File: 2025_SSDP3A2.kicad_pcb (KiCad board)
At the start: 4 copper layers, 58.4 x 28.8 mm, 64 parts, among them J1 SolderPad, J2 SolderPad, J3 SolderPad, J4 SolderPad, J5 SolderPad, J6 SolderPad, J7 SolderPad_01x06, Q1 IAUZ30N10S5L240, Q2 BSZ096N10LS5, U1 LM5146RGYR

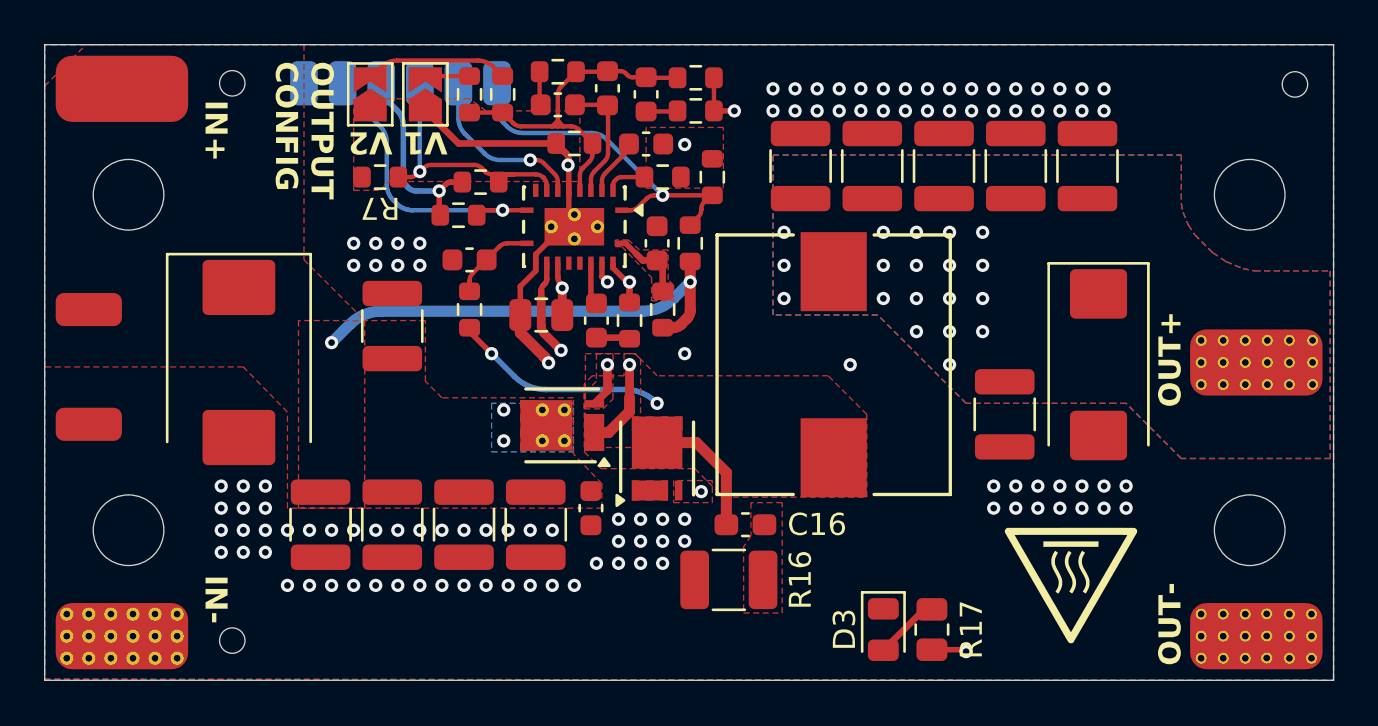
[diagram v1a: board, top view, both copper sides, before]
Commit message: Improvements to copper, EMI reduction techniques
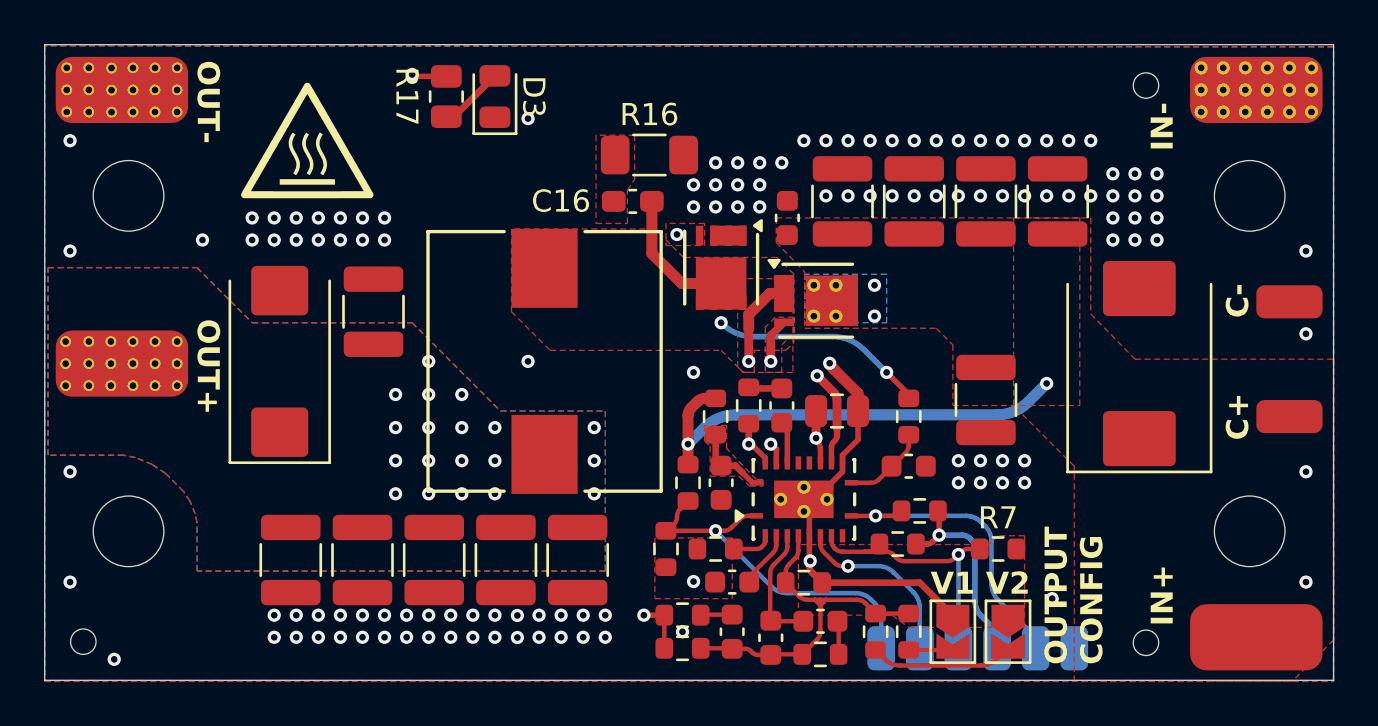
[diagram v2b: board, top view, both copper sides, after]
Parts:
- R16: footprint Resistor_SMD:R_1210_3225Metric_Pad1.30x2.65mm_HandSolder -> Resistor_SMD:R_1206_3216Metric_Pad1.30x1.75mm_HandSolder
- moved H5 60.4 mm to (121.8, 127.0), turned to 180 degrees
- moved J1 57.1 mm to (174.9, 126.8), turned to -90 degrees
- moved J4 57.0 mm to (174.9, 102.0), turned to -90 degrees
- moved J6 57.0 mm to (123.5, 102.0), turned to 90 degrees
- moved J3 54.7 mm to (176.4, 111.7), turned to -90 degrees
- moved J2 54.6 mm to (176.4, 116.8), turned to -90 degrees
- moved H1 53.0 mm to (174.6, 122.0), turned to 180 degrees
- moved H3 53.0 mm to (123.8, 122.0), turned to 180 degrees
- moved H2 53.0 mm to (174.6, 106.8), turned to 180 degrees
- moved H4 53.0 mm to (123.8, 106.8), turned to 180 degrees
- moved J5 51.4 mm to (123.5, 114.5), turned to 90 degrees
- moved H6 48.5 mm to (169.9, 127.1), turned to 180 degrees
- moved H7 48.4 mm to (169.9, 101.8), turned to 180 degrees
- moved D1 40.8 mm to (169.6, 114.5), turned to 90 degrees
- moved C22 40.3 mm to (131.2, 123.3), turned to -90 degrees
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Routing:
- net PGND: vias 108 -> 121
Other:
- board text added: "C+"
- board text added: "C-"
- board text added: "INPUT: 20-60V⎓4A OUTPUT: 5.1-12V⎓8A"
- board text removed: "INPUT: 20-70V⎓4A OUTPUT: 5.1-12V⎓8A"

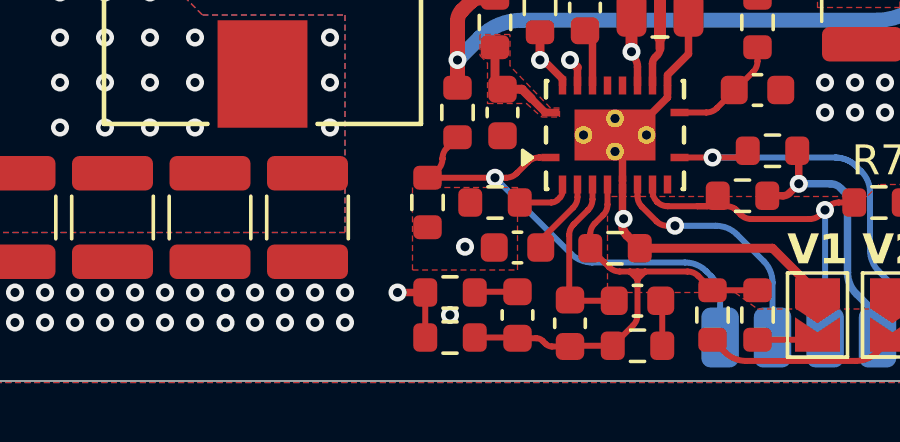
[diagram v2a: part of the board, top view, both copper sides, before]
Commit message: Updated schematic, added more silkscreen markings
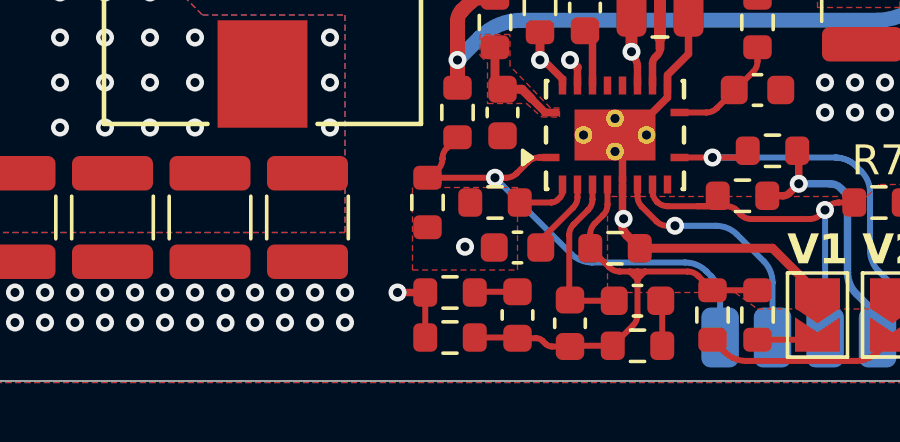
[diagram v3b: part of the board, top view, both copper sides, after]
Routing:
- net PGND: vias 121 -> 120
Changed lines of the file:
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@@
-	)
-	(via
-		(at 148.9 126.6)
-		(size 0.6)
-		(drill 0.3)
-		(layers "F.Cu" "B.Cu")
-		(free yes)
-		(net 1)
 	)
 	(via

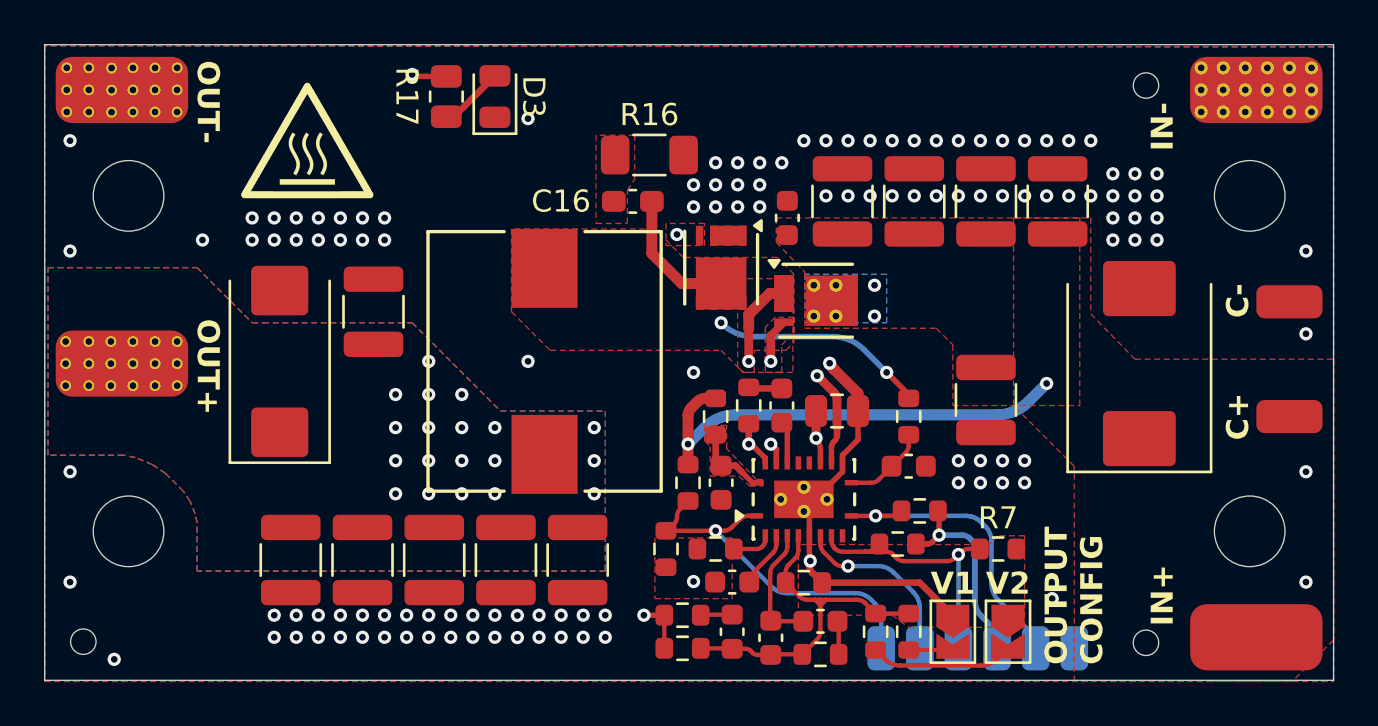
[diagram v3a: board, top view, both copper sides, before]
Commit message: Added more thermal area
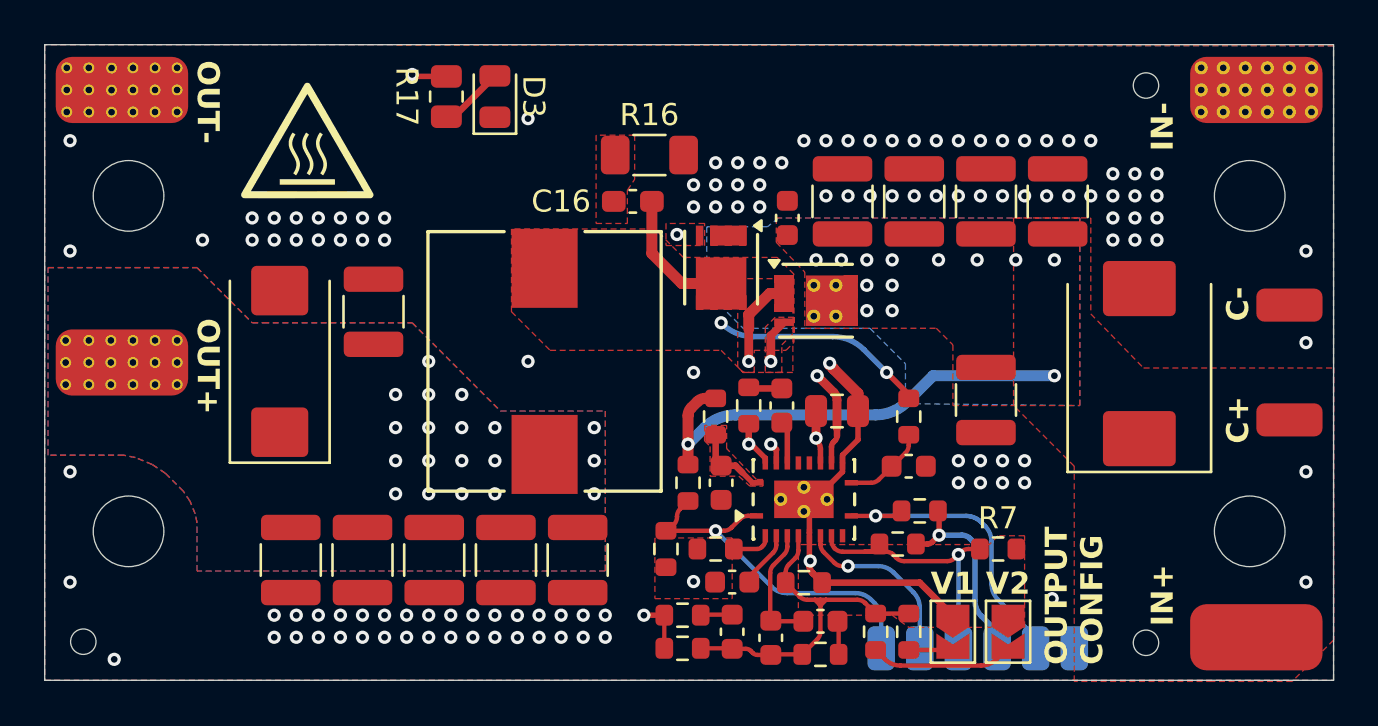
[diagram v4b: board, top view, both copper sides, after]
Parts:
- moved J2 0.15 mm to (176.4, 117.0)
- moved J3 0.15 mm to (176.4, 111.8)
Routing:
- net VBAT: track 21.1 -> 21.6 mm, vias 4 -> 14
- removed copper zone on In1.Cu, net VBAT
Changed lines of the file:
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@@
 	(footprint "Connector_Wire:SolderWirePad_1x01_SMD_1.5x3mm"
 		(layer "F.Cu")
-		(at 176.4 116.85 -90)
+		(at 176.4 117 -90)
 		(descr "Wire Pad, Square, SMD Pad,  1.5mm x 3mm")
 		(tags "MeasurementPoint Square SMDPad 1.5mmx3mm ")
@@
 		(locked yes)
 		(layer "F.Cu")
-		(at 123.5 114.45 90)
+		(at 123.5 114.4 90)
 		(descr "Wire Pad, Square, SMD Pad,  3mm x 6mm")
 		(tags "MeasurementPoint Square SMDPad 3mmx6mm ")
@@
 	(footprint "Connector_Wire:SolderWirePad_1x01_SMD_1.5x3mm"
 		(layer "F.Cu")
-		(at 176.4 111.65 -90)
+		(at 176.4 111.8 -90)
 		(descr "Wire Pad, Square, SMD Pad,  1.5mm x 3mm")
 		(tags "MeasurementPoint Square SMDPad 1.5mmx3mm ")
@@
 	)
 	(gr_rect
-		(start 177.35 116.1)
-		(end 178.45 117.6)
+		(start 177.35 116.25)
+		(end 178.45 117.75)
 		(stroke
 			(width 0.001)
@@
 	)
 	(gr_rect
-		(start 120 112.95)
-		(end 123 115.95)
+		(start 120 112.9)
+		(end 123 115.9)
 		(stroke
 			(width 0.001)
@@
 	)
 	(gr_rect
-		(start 177.35 110.9)
-		(end 178.45 112.4)
+		(start 177.35 111.05)
+		(end 178.45 112.55)
 		(stroke
 			(width 0.001)
@@
 	)
 	(gr_line
-		(start 178.9 114.25)
-		(end 179.4 114.25)
+		(start 178.9 114.4)
+		(end 179.4 114.4)
 		(stroke
 			(width 0.1)
@@
 	(gr_rect
 		(start 120 100)
-		(end 178.4 128.85)
+		(end 178.4 128.8)
 		(stroke
 			(width 0.1)
@@
 	)
 	(gr_rect
-		(start 178.9 109.25)
-		(end 192.9 119.25)
+		(start 178.9 109.4)
+		(end 192.9 119.4)
 		(stroke
 			(width 0.1)
@@
 	)
 	(gr_text "OUT+"
-		(at 127.4 114.6 270)
+		(at 127.4 114.575 270)
 		(layer "F.SilkS")
 		(effects
@@
 	)
 	(gr_text "C+"
-		(at 174.65 116.85 90)
+		(at 174.65 117 90)
 		(layer "F.SilkS")
 		(effects
@@
 	)
 	(gr_text "C-"
-		(at 174.65 111.6 90)
+		(at 174.65 111.75 90)
 		(layer "F.SilkS")
 		(effects
@@
 	)
 	(via
-		(at 177.15 113.1)
+		(at 177.15 113.5)
 		(size 0.6)
 		(drill 0.3)
@@
 	)
 	(via
-		(at 157.6 110.9)
+		(at 160.5 109.75)
 		(size 0.6)
 		(drill 0.3)
@@
 		(keep_end_layers yes)
 		(free yes)
-		(zone_layer_connections "In1.Cu" "In2.Cu")
+		(zone_layer_connections "In2.Cu")
+		(net 24)
+	)
+	(via
+		(at 158.4 109.75)
+		(size 0.6)
+		(drill 0.3)
+		(layers "F.Cu" "B.Cu")
+		(free yes)
+		(net 24)
+	)
+	(via
+		(at 157.25 110.9)
+		(size 0.6)
+		(drill 0.3)
+		(layers "F.Cu" "B.Cu")
+		(free yes)
+		(net 24)
+	)
+	(via
+		(at 158.4 110.9)
+		(size 0.6)
+		(drill 0.3)
+		(layers "F.Cu" "B.Cu")
+		(free yes)
+		(net 24)
+	)
+	(via
+		(at 165.75 109.75)
+		(size 0.6)
+		(drill 0.3)
+		(layers "F.Cu" "B.Cu")
+		(remove_unused_layers yes)
+		(keep_end_layers yes)
+		(free yes)
+		(zone_layer_connections "In2.Cu")
+		(net 24)
+	)
+	(via
+		(at 158.4 112.05)
+		(size 0.6)
+		(drill 0.3)
+		(layers "F.Cu" "B.Cu")
+		(free yes)
 		(net 24)
 	)
@@
 	)
 	(via
-		(at 157.6 112.3)
+		(at 157.25 109.75)
+		(size 0.6)
+		(drill 0.3)
+		(layers "F.Cu" "B.Cu")
+		(free yes)
+		(net 24)
+	)
+	(via
+		(at 157.25 112.05)
+		(size 0.6)
+		(drill 0.3)
+		(layers "F.Cu" "B.Cu")
+		(free yes)
+		(net 24)
+	)
+	(via
+		(at 162.25 109.75)
 		(size 0.6)
 		(drill 0.3)
@@
 		(keep_end_layers yes)
 		(free yes)
-		(zone_layer_connections "In1.Cu" "In2.Cu")
+		(zone_layer_connections "In2.Cu")
 		(net 24)
 	)
 	(via
-		(at 165.4 115.35)
+		(at 165.75 115)
 		(size 0.6)
 		(drill 0.3)
@@
 		(keep_end_layers yes)
 		(free yes)
-		(zone_layer_connections)
+		(zone_layer_connections "In2.Cu")
+		(net 24)
+	)
+	(via
+		(at 156.1 109.75)
+		(size 0.6)
+		(drill 0.3)
+		(layers "F.Cu" "B.Cu")
+		(free yes)
+		(net 24)
+	)
+	(via
+		(at 164 109.75)
+		(size 0.6)
+		(drill 0.3)
+		(layers "F.Cu" "B.Cu")
+		(remove_unused_layers yes)
+		(keep_end_layers yes)
+		(free yes)
+		(zone_layer_connections "In2.Cu")
+		(net 24)
+	)
+	(via
+		(at 154.95 109.75)
+		(size 0.6)
+		(drill 0.3)
+		(layers "F.Cu" "B.Cu")
+		(free yes)
 		(net 24)
 	)
@@
 	)
 	(segment
-		(start 165.4 115.35)
-		(end 164.561786 116.188214)
+		(start 151.304427 116.774)
+		(end 157.647573 116.774)
 		(width 0.5)
 		(layer "B.Cu")
@@
 	)
 	(segment
-		(start 149.890213 117.359787)
-		(end 149.15 118.1)
+		(start 159.061786 116.188214)
+		(end 160.25 115)
 		(width 0.5)
 		(layer "B.Cu")
@@
 	)
 	(segment
-		(start 151.304427 116.774)
-		(end 163.147573 116.774)
+		(start 149.15 118.1)
+		(end 149.890213 117.359787)
 		(width 0.5)
 		(layer "B.Cu")
 		(net 24)
 	)
-	(arc
-		(start 164.561786 116.188214)
-		(mid 163.91294 116.621759)
-		(end 163.147573 116.774)
+	(segment
+		(start 160.25 115)
+		(end 165.75 115)
 		(width 0.5)
 		(layer "B.Cu")
@@
 		(net 24)
 	)
+	(arc
+		(start 157.647573 116.774)
+		(mid 158.41294 116.621759)
+		(end 159.061786 116.188214)
+		(width 0.5)
+		(layer "B.Cu")
+		(net 24)
+	)
 	(segment
 		(start 159.15 127.425)
@@
 		(priority 3)
 		(connect_pads yes
-			(clearance 0.25)
+			(clearance 0.5)
 		)
 		(min_thickness 0.25)
@@
 	)
 	(zone
-		(net 24)
-		(net_name "VBAT")
-		(layer "F.Cu")
-		(name "TZVIN")
-		(hatch edge 0.5)
-		(priority 2)
-		(connect_pads yes
-			(clearance 0.25)
-		)
-		(min_thickness 0.25)
-		(filled_areas_thickness no)
-		(fill yes
-			(thermal_gap 0.5)
-			(thermal_bridge_width 0.5)
-		)
-		(polygon
-			(pts
-				(xy 166.9 116.35) (xy 166.9 107.85) (xy 153.15 107.85) (xy 153.15 108.954645) (xy 154.44 110.304644)
-				(xy 154.44 112.85) (xy 160.4 112.85) (xy 161.15 113.6) (xy 161.15 116.35)
-			)
-		)
-	)
-	(zone
 		(net 0)
 		(net_name "")
@@
 			(pts
 				(xy 178.4 126.975) (xy 176.525 128.85) (xy 172.9 128.85) (xy 166.65 128.85) (xy 166.65 119.1) (xy 163.9 116.35)
-				(xy 163.9 107.85) (xy 167.4 107.85) (xy 167.4 112.2) (xy 169.4 114.25) (xy 178.4 114.25) (xy 178.4 119.05)
+				(xy 163.9 107.85) (xy 167.4 107.85) (xy 167.4 112.2) (xy 169.790244 114.65) (xy 178.4 114.65) (xy 178.4 119.05)
 				(xy 178.4 125.05)
 			)
@@
 		(polygon
 			(pts
-				(xy 178.4 128.85) (xy 178.4 100.1) (xy 120 100.05) (xy 120 128.85)
+				(xy 178.4 128.8) (xy 178.4 100.05) (xy 120 100) (xy 120 128.8)
 			)
 		)
@@
 		(net 24)
 		(net_name "VBAT")
-		(layers "B.Cu" "In1.Cu" "In2.Cu")
-		(name "INTZBAT")
+		(layers "F.Cu" "In2.Cu")
+		(name "TZVIN")
 		(hatch edge 0.5)
-		(priority 6)
+		(priority 2)
+		(connect_pads yes
+			(clearance 0.25)
+		)
+		(min_thickness 0.25)
+		(filled_areas_thickness no)
+		(fill yes
+			(thermal_gap 0.5)
+			(thermal_bridge_width 0.5)
+		)
+		(polygon
+			(pts
+				(xy 166.9 116.35) (xy 166.9 107.85) (xy 153.15 107.85) (xy 153.15 108.954645) (xy 154.44 110.304644)
+				(xy 154.44 112.85) (xy 160.4 112.85) (xy 161.15 113.6) (xy 161.15 116.35)
+			)
+		)
+	)
+	(zone
+		(net 24)
+		(net_name "VBAT")
+		(layer "B.Cu")
+		(name "TZVIN2")
+		(hatch edge 0.5)
+		(priority 2)
 		(connect_pads yes
 			(clearance 0.25)
@@
 			(thermal_gap 0.5)
 			(thermal_bridge_width 0.5)
-			(smoothing fillet)
-			(radius 0.5)
 		)
 		(polygon
 			(pts
-				(xy 158.15 112.6) (xy 158.15 110.4) (xy 154.45 110.4) (xy 154.45 112.6)
+				(xy 166.9 116.353615) (xy 166.9 107.853615) (xy 153.25 107.853615) (xy 152.75 108.25) (xy 150 108.25)
+				(xy 150 111.202712) (xy 151.650903 112.853615) (xy 157.397365 112.853615) (xy 159 114.45625) (xy 159 116.264155)
 			)
 		)

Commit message: Added TVS protection to aux IO
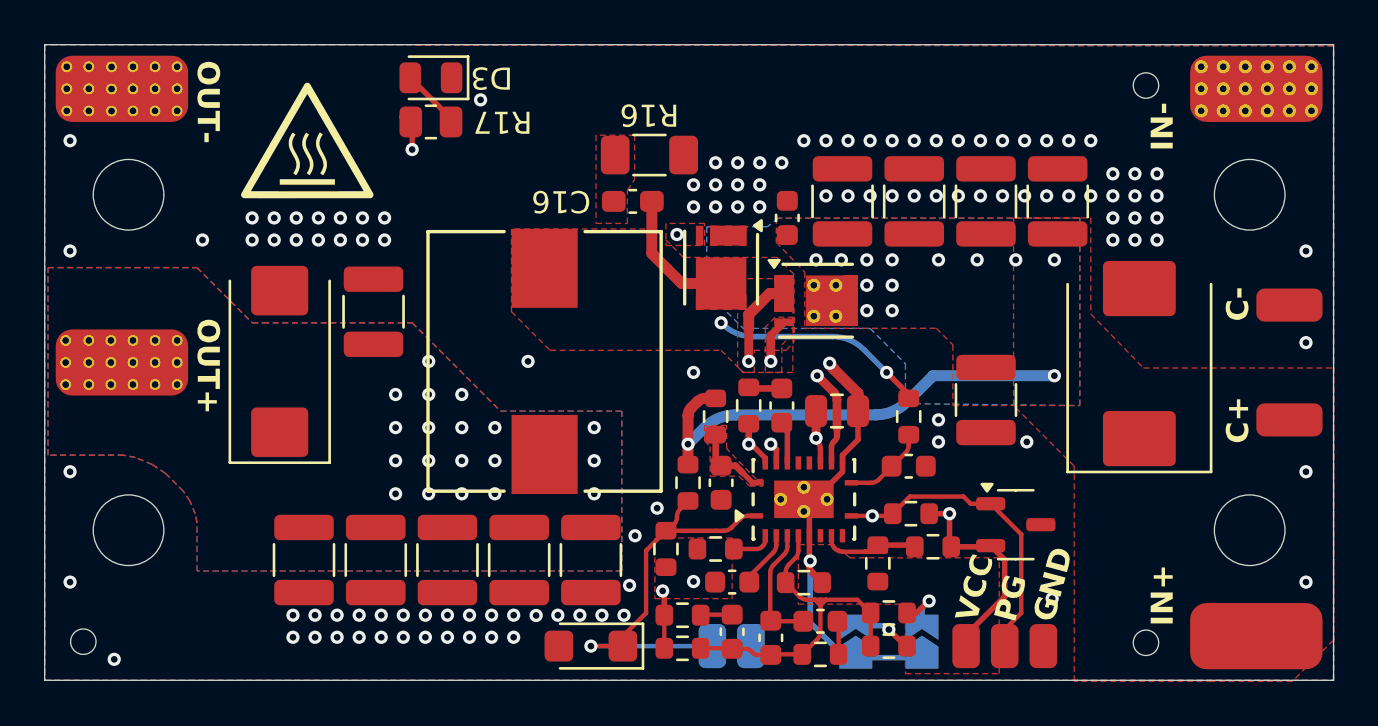
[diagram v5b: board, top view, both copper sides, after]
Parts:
- added D4: SMF58A, Diode_SMD:D_SMF, F.Cu at (144.8, 127.2)
- added D5: 8V, Package_TO_SOT_SMD:SOT-23-3, F.Cu at (164.0, 121.8)
- added J8: SolderPad_1x03, Connector_Custom:SolderWirePad_1x03_SMD_1.5x2mm, F.Cu at (161.5, 127.2)
- J7: value SolderPad_01x06 -> SolderPad_01x02; footprint Connector_Custom:SolderWirePad_1x06_SMD_1.5x2mm -> Connector_Custom:SolderWirePad_1x02_SMD_1.5x2mm
- JP1, JP2: moved to B.Cu
- R16: value 1 -> 0
- moved J7 9.40 mm to (150.0, 127.2)
- moved JP2 6.91 mm to (156.8, 127.0), turned to 90 degrees
- moved R7 5.49 mm to (157.8, 123.5), turned to -90 degrees
- moved D3 3.02 mm to (137.5, 101.5), turned to 180 degrees
- moved R5 1.60 mm to (160.2, 122.8)
- moved JP1 1.47 mm to (159.8, 127.0), turned to 90 degrees
- moved R17 1.35 mm to (137.5, 103.5), turned to 0 degrees
- moved R11 1.24 mm to (158.2, 125.8), turned to 0 degrees
- moved R12 0.88 mm to (158.2, 127.2), turned to 0 degrees
- moved C17 0.60 mm to (141.5, 123.3)
- moved C18 0.60 mm to (138.2, 123.3)
- moved C19 0.60 mm to (135.0, 123.3)
- moved C20 0.60 mm to (144.8, 123.3)
- moved C22 0.60 mm to (131.8, 123.3)
- moved R4 0.42 mm to (159.2, 121.2)
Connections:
- J7 pad 1: SYNCOUT -> U1_EN
- J7 pad 2: SYNCIN -> PGND
- R5 pad 2: SYNCIN -> /SYNCIN
- R7 pad 1: SYNCIN -> /SYNCIN
- U1 pad 7: SYNCOUT -> unconnected-(U1-SYNCOUT-Pad7)
- U1 pad 8: SYNCIN -> /SYNCIN
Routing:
- net SYNCIN: track 12.5 -> 0.00 mm, vias 1 -> 0
- net SYNCOUT: track 7.89 -> 0.00 mm, vias 1 -> 0
- net /SYNCIN: track 0.00 -> 5.50 mm
- net /JP_CFG2: track 6.53 -> 2.71 mm, vias 0 -> 1
- net U1_EN: track 16.4 -> 19.1 mm
- net VOUT: track 42.7 -> 40.1 mm
- net AGND: track 14.6 -> 16.6 mm
- net VCC: track 18.7 -> 19.9 mm
- net /JP_CFG1: track 2.04 -> 2.38 mm, vias 0 -> 1
- net PGND: vias 120 -> 113
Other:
- board text removed: "SYNC_I"
- board text removed: "SYNC_O"
